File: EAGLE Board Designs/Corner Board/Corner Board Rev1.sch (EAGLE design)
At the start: 7 parts, among them J1 CONNECTOR-4_μF_T_V_BLACK, J2 CONNECTOR-2_MOLEX_NANOFIT_PTH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, J3 CONNECTOR-10_MF_T_V_, J4 CONNECTOR-4_μF_T_V_BLACK, J5 CONNECTOR-4_μF_T_V_BLACK, U1 VOLTAGE_REGULATOR_SOT-89_15V, U2 OPAMP_1_CHANNEL_OPA991

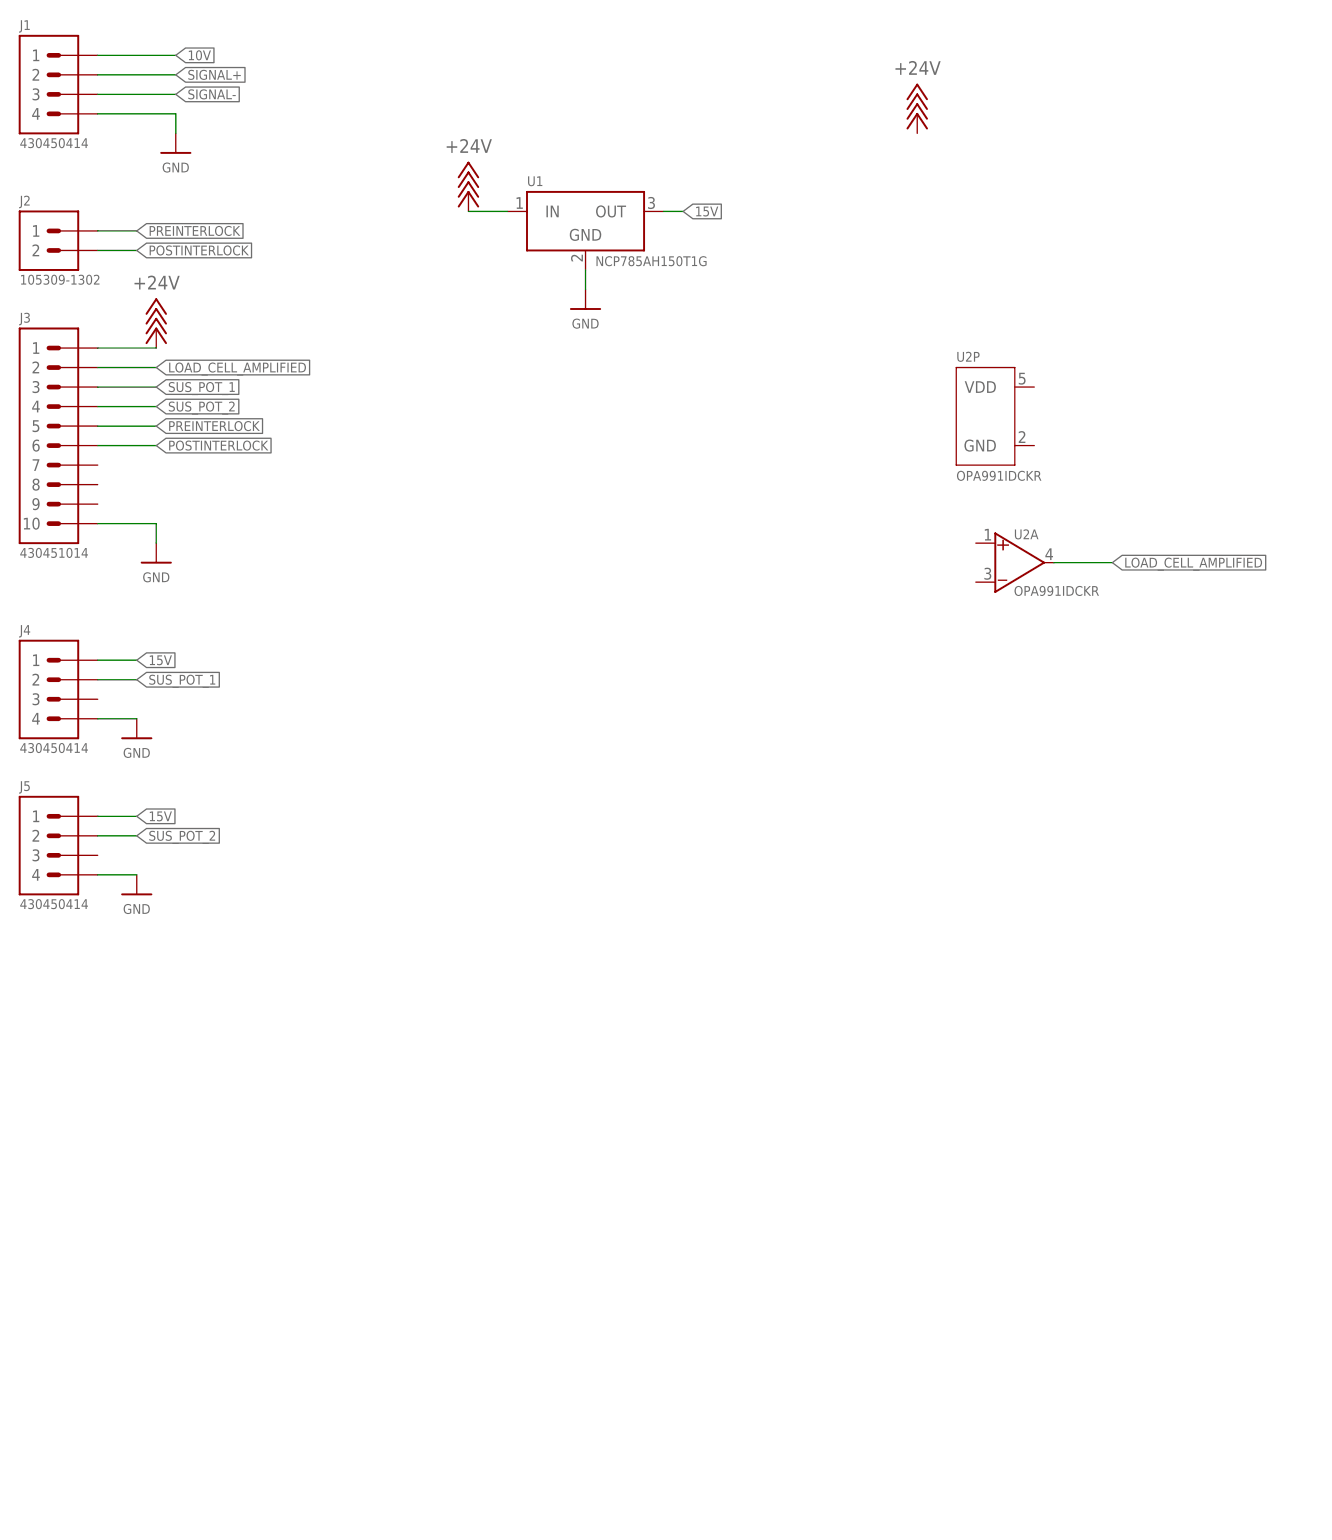
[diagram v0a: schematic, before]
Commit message: added op amps
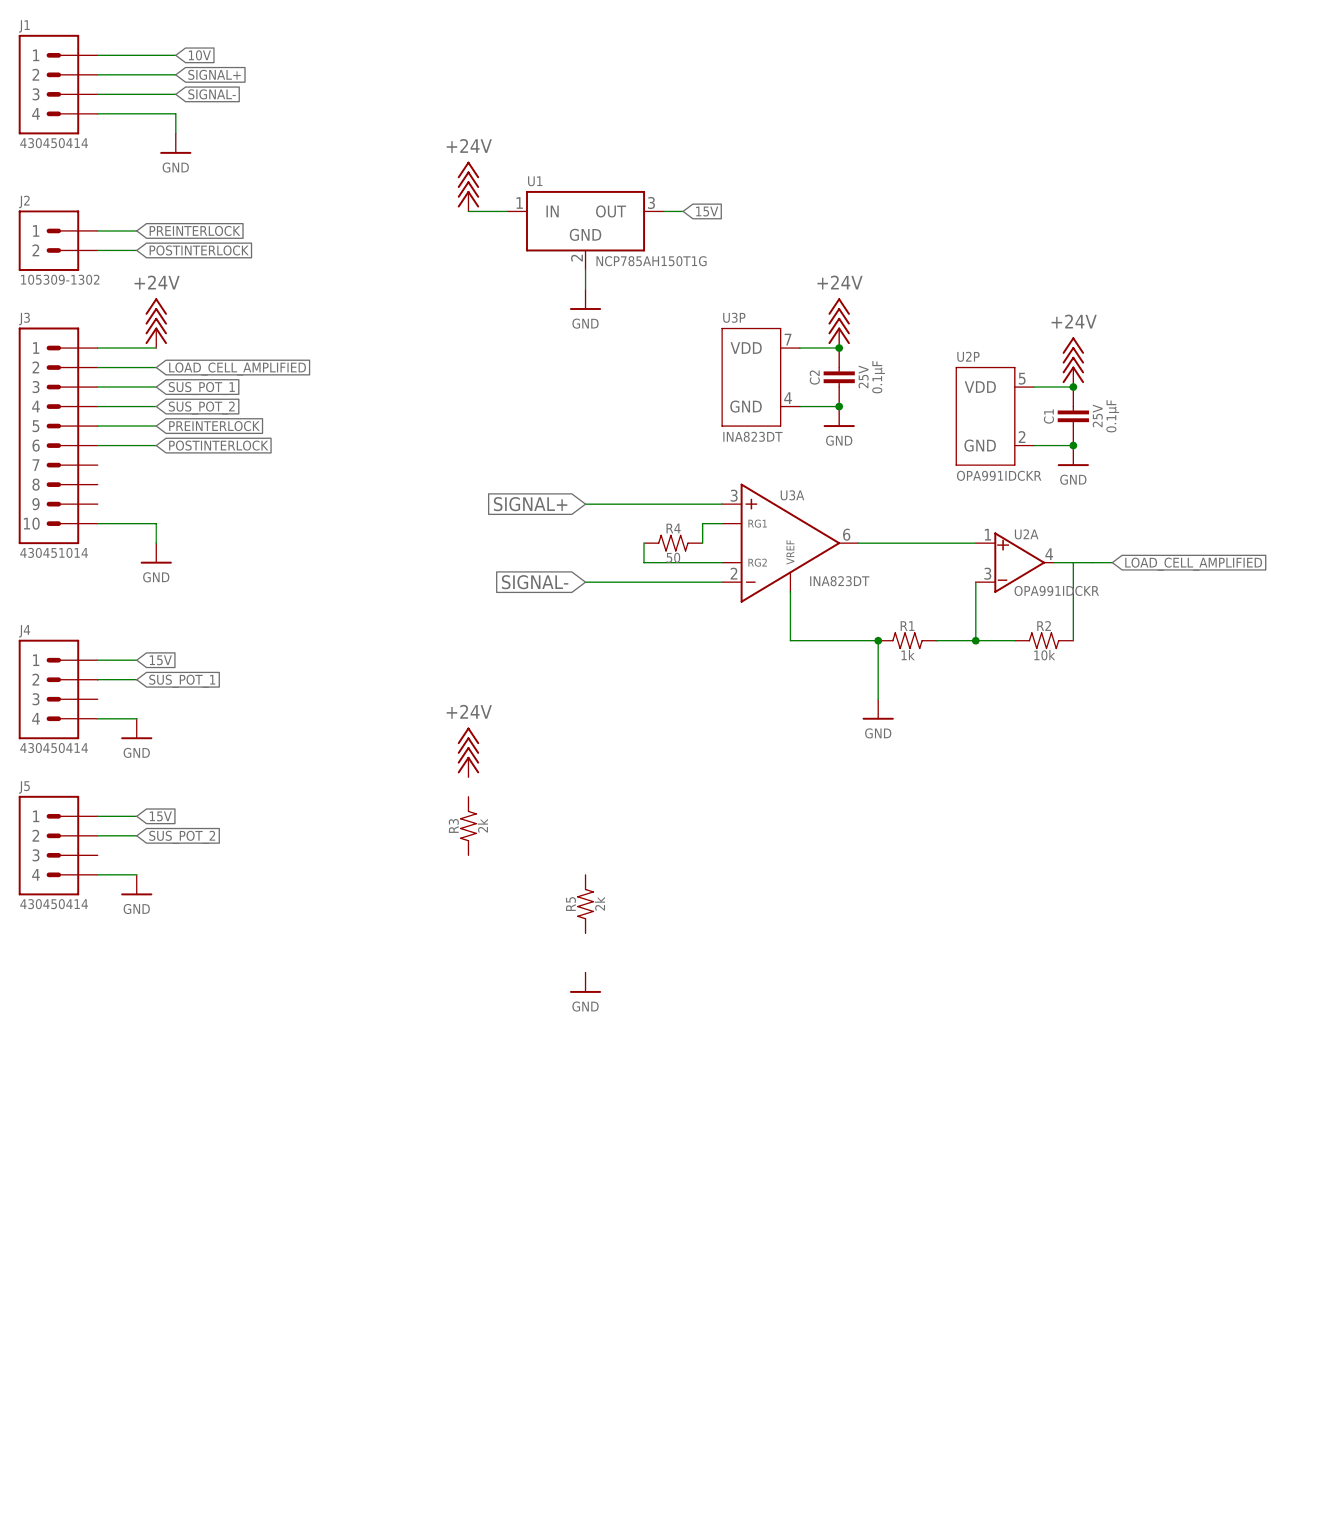
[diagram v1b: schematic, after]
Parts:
- added C1, C2: CAPACITOR_0603_25V_0.1UF, HyTechDevices:CAPACITOR_0603_25V_0.1UF
- added R1: RESISTOR_0603_1K, HyTechDevices:RESISTOR_0603_1K
- added R2: RESISTOR_0603_10K, HyTechDevices:RESISTOR_0603_10K
- added R3, R5: RESISTOR_0603_2K, HyTechDevices:RESISTOR_0603_2K
- added R4: RESISTOR_0603_50, HyTechDevices:RESISTOR_0603_50
- added U3: INA823DT, HyTechDevices:INA823DT
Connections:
- new net N$1: R1.2, R2.1, U2A.VIN-
- new net N$2: R4.2, U3A.RG1
- new net N$3: U2A.VIN+, U3A.VOUT
- new net N$4: R4.1, U3A.RG2
- net +24V: now also C1.1, C2.1, U2P.VDD, U3P.VDD
- net GND: now also C1.2, C2.2, R1.1, U2P.GND, U3A.VREF, U3P.GND
- net LOAD_CELL_AMPLIFIED: now also R2.2
- net SIGNAL+: now also U3A.VIN+
- net SIGNAL-: now also U3A.VIN-
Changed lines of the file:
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@@
 <part name="U2" library="HyTechDevices" deviceset="OPAMP_1_CHANNEL_*" device="" technology="OPA991"/>
 <part name="U$3" library="HyTechSupplies" deviceset="+24V" device=""/>
+<part name="R1" library="HyTechDevices" deviceset="RESISTOR_?_*" device="0603" technology="1K"/>
+<part name="R2" library="HyTechDevices" deviceset="RESISTOR_?_*" device="0603" technology="10K"/>
+<part name="P6" library="HyTechSupplies" deviceset="GND" device=""/>
+<part name="P7" library="HyTechSupplies" deviceset="GND" device=""/>
+<part name="U$4" library="HyTechSupplies" deviceset="+24V" device=""/>
+<part name="C1" library="HyTechDevices" deviceset="CAPACITOR_?_*" device="0603" technology="25V_0.1UF"/>
+<part name="U3" library="HyTechDevices" deviceset="INA823*" device="" technology="DT"/>
+<part name="R3" library="HyTechDevices" deviceset="RESISTOR_?_*" device="0603" technology="2K"/>
+<part name="R4" library="HyTechDevices" deviceset="RESISTOR_?_*" device="0603" technology="50"/>
+<part name="P8" library="HyTechSupplies" deviceset="GND" device=""/>
+<part name="U$5" library="HyTechSupplies" deviceset="+24V" device=""/>
+<part name="C2" library="HyTechDevices" deviceset="CAPACITOR_?_*" device="0603" technology="25V_0.1UF"/>
+<part name="R5" library="HyTechDevices" deviceset="RESISTOR_?_*" device="0603" technology="2K"/>
+<part name="P9" library="HyTechSupplies" deviceset="GND" device=""/>
 </parts>
 <sheets>
@@
 <attribute name="MPN" x="127" y="22.098" size="1.27" layer="95" align="top-left"/>
 </instance>
-<instance part="U$3" gate="G$1" x="121.92" y="68.58" smashed="yes">
-<attribute name="VALUE" x="121.92" y="73.66" size="1.778" layer="96" align="bottom-center"/>
+<instance part="U$3" gate="G$1" x="63.5" y="-15.24" smashed="yes">
+<attribute name="VALUE" x="63.5" y="-10.16" size="1.778" layer="96" align="bottom-center"/>
+</instance>
+<instance part="R1" gate="G$1" x="121.92" y="0" smashed="yes">
+<attribute name="NAME" x="120.65" y="1.27" size="1.27" layer="95" align="bottom-center"/>
+<attribute name="RESISTANCE" x="120.65" y="-1.27" size="1.27" layer="96" align="top-center"/>
+</instance>
+<instance part="R2" gate="G$1" x="139.7" y="0" smashed="yes">
+<attribute name="NAME" x="138.43" y="1.27" size="1.27" layer="95" align="bottom-center"/>
+<attribute name="RESISTANCE" x="138.43" y="-1.27" size="1.27" layer="96" align="top-center"/>
+</instance>
+<instance part="P6" gate="1" x="116.84" y="-10.16" smashed="yes">
+<attribute name="VALUE" x="116.84" y="-11.43" size="1.27" layer="96" align="top-center"/>
+</instance>
+<instance part="P7" gate="1" x="142.24" y="22.86" smashed="yes">
+<attribute name="VALUE" x="142.24" y="21.59" size="1.27" layer="96" align="top-center"/>
+</instance>
+<instance part="U$4" gate="G$1" x="142.24" y="35.56" smashed="yes">
+<attribute name="VALUE" x="142.24" y="40.64" size="1.778" layer="96" align="bottom-center"/>
+</instance>
+<instance part="C1" gate="G$1" x="142.24" y="30.48" smashed="yes" rot="R90">
+<attribute name="NAME" x="139.7" y="29.21" size="1.27" layer="95" rot="R90" align="bottom-center"/>
+<attribute name="VOLTAGE" x="144.78" y="29.21" size="1.27" layer="96" rot="R90" align="top-center"/>
+<attribute name="CAPACITANCE" x="146.558" y="29.21" size="1.27" layer="96" rot="R90" align="top-center"/>
+</instance>
+<instance part="U3" gate="A" x="99.06" y="12.7" smashed="yes">
+<attribute name="NAME" x="104.013" y="18.288" size="1.27" layer="95"/>
+<attribute name="MPN" x="107.823" y="8.382" size="1.27" layer="96" align="top-left"/>
+</instance>
+<instance part="U3" gate="P" x="96.52" y="40.64" smashed="yes">
+<attribute name="NAME" x="96.52" y="41.402" size="1.27" layer="95"/>
+<attribute name="MPN" x="96.52" y="27.178" size="1.27" layer="95" align="top-left"/>
+</instance>
+<instance part="R3" gate="G$1" x="63.5" y="-22.86" smashed="yes" rot="R90">
+<attribute name="NAME" x="62.23" y="-24.13" size="1.27" layer="95" rot="R90" align="bottom-center"/>
+<attribute name="RESISTANCE" x="64.77" y="-24.13" size="1.27" layer="96" rot="R90" align="top-center"/>
+</instance>
+<instance part="R4" gate="G$1" x="91.44" y="12.7" smashed="yes">
+<attribute name="NAME" x="90.17" y="13.97" size="1.27" layer="95" align="bottom-center"/>
+<attribute name="RESISTANCE" x="90.17" y="11.43" size="1.27" layer="96" align="top-center"/>
+</instance>
+<instance part="P8" gate="1" x="111.76" y="27.94" smashed="yes">
+<attribute name="VALUE" x="111.76" y="26.67" size="1.27" layer="96" align="top-center"/>
+</instance>
+<instance part="U$5" gate="G$1" x="111.76" y="40.64" smashed="yes">
+<attribute name="VALUE" x="111.76" y="45.72" size="1.778" layer="96" align="bottom-center"/>
+</instance>
+<instance part="C2" gate="G$1" x="111.76" y="35.56" smashed="yes" rot="R90">
+<attribute name="NAME" x="109.22" y="34.29" size="1.27" layer="95" rot="R90" align="bottom-center"/>
+<attribute name="VOLTAGE" x="114.3" y="34.29" size="1.27" layer="96" rot="R90" align="top-center"/>
+<attribute name="CAPACITANCE" x="116.078" y="34.29" size="1.27" layer="96" rot="R90" align="top-center"/>
+</instance>
+<instance part="R5" gate="G$1" x="78.74" y="-33.02" smashed="yes" rot="R90">
+<attribute name="NAME" x="77.47" y="-34.29" size="1.27" layer="95" rot="R90" align="bottom-center"/>
+<attribute name="RESISTANCE" x="80.01" y="-34.29" size="1.27" layer="96" rot="R90" align="top-center"/>
+</instance>
+<instance part="P9" gate="1" x="78.74" y="-45.72" smashed="yes">
+<attribute name="VALUE" x="78.74" y="-46.99" size="1.27" layer="96" align="top-center"/>
 </instance>
 </instances>
@@
 <pinref part="P5" gate="1" pin="GND"/>
 </segment>
+<segment>
+<pinref part="R1" gate="G$1" pin="1"/>
+<wire x1="116.84" y1="0" x2="116.84" y2="-7.62" width="0.1524" layer="91"/>
+<pinref part="P6" gate="1" pin="GND"/>
+<pinref part="U3" gate="A" pin="VREF"/>
+<wire x1="105.41" y1="6.35" x2="105.41" y2="0" width="0.1524" layer="91"/>
+<wire x1="105.41" y1="0" x2="116.84" y2="0" width="0.1524" layer="91"/>
+<junction x="116.84" y="0"/>
+</segment>
+<segment>
+<pinref part="P7" gate="1" pin="GND"/>
+<pinref part="C1" gate="G$1" pin="2"/>
+<pinref part="U2" gate="P" pin="GND"/>
+<wire x1="137.16" y1="25.4" x2="142.24" y2="25.4" width="0.1524" layer="91"/>
+<junction x="142.24" y="25.4"/>
+</segment>
+<segment>
+<pinref part="P8" gate="1" pin="GND"/>
+<pinref part="C2" gate="G$1" pin="2"/>
+<wire x1="106.68" y1="30.48" x2="111.76" y2="30.48" width="0.1524" layer="91"/>
+<junction x="111.76" y="30.48"/>
+<pinref part="U3" gate="P" pin="GND"/>
+</segment>
 </net>
 <net name="SIGNAL+" class="0">
@@
 <label x="25.4" y="73.66" size="1.27" layer="95" xref="yes"/>
 </segment>
+<segment>
+<pinref part="U3" gate="A" pin="VIN+"/>
+<wire x1="96.52" y1="17.78" x2="78.74" y2="17.78" width="0.1524" layer="91"/>
+<label x="78.74" y="17.78" size="1.778" layer="95" rot="R180" xref="yes"/>
+</segment>
 </net>
 <net name="SIGNAL-" class="0">
@@
 <label x="25.4" y="71.12" size="1.27" layer="95" xref="yes"/>
 </segment>
+<segment>
+<pinref part="U3" gate="A" pin="VIN-"/>
+<wire x1="96.52" y1="7.62" x2="78.74" y2="7.62" width="0.1524" layer="91"/>
+<label x="78.74" y="7.62" size="1.778" layer="95" rot="R180" xref="yes"/>
+</segment>
 </net>
 <net name="PREINTERLOCK" class="0">
@@
 <pinref part="U$2" gate="G$1" pin="+24V"/>
 </segment>
+<segment>
+<pinref part="U$4" gate="G$1" pin="+24V"/>
+<pinref part="C1" gate="G$1" pin="1"/>
+<pinref part="U2" gate="P" pin="VDD"/>
+<wire x1="137.16" y1="33.02" x2="142.24" y2="33.02" width="0.1524" layer="91"/>
+<junction x="142.24" y="33.02"/>
+</segment>
+<segment>
+<pinref part="U$5" gate="G$1" pin="+24V"/>
+<pinref part="C2" gate="G$1" pin="1"/>
+<wire x1="106.68" y1="38.1" x2="111.76" y2="38.1" width="0.1524" layer="91"/>
+<junction x="111.76" y="38.1"/>
+<pinref part="U3" gate="P" pin="VDD"/>
+</segment>
 </net>
 <net name="LOAD_CELL_AMPLIFIED" class="0">
@@
 <segment>
 <pinref part="U2" gate="A" pin="VOUT"/>
-<wire x1="139.7" y1="10.16" x2="147.32" y2="10.16" width="0.1524" layer="91"/>
+<wire x1="139.7" y1="10.16" x2="142.24" y2="10.16" width="0.1524" layer="91"/>
 <label x="147.32" y="10.16" size="1.27" layer="95" xref="yes"/>
+<pinref part="R2" gate="G$1" pin="2"/>
+<wire x1="144.78" y1="10.16" x2="147.32" y2="10.16" width="0.1524" layer="91"/>
+<wire x1="144.78" y1="10.16" x2="142.24" y2="10.16" width="0.1524" layer="91"/>
+<wire x1="142.24" y1="10.16" x2="142.24" y2="0" width="0.1524" layer="91"/>
 </segment>
 </net>
@@
 </segment>
 </net>
+<net name="N$1" class="0">
+<segment>
+<pinref part="U2" gate="A" pin="VIN-"/>
+<wire x1="129.54" y1="7.62" x2="129.54" y2="0" width="0.1524" layer="91"/>
+<pinref part="R2" gate="G$1" pin="1"/>
+<wire x1="129.54" y1="0" x2="134.62" y2="0" width="0.1524" layer="91"/>
+<pinref part="R1" gate="G$1" pin="2"/>
+<wire x1="129.54" y1="0" x2="124.46" y2="0" width="0.1524" layer="91"/>
+<junction x="129.54" y="0"/>
+</segment>
+</net>
+<net name="N$3" class="0">
+<segment>
+<pinref part="U2" gate="A" pin="VIN+"/>
+<wire x1="129.54" y1="12.7" x2="114.3" y2="12.7" width="0.1524" layer="91"/>
+<pinref part="U3" gate="A" pin="VOUT"/>
+</segment>
+</net>
+<net name="N$2" class="0">
+<segment>
+<pinref part="R4" gate="G$1" pin="2"/>
+<pinref part="U3" gate="A" pin="RG1"/>
+<wire x1="93.98" y1="12.7" x2="93.98" y2="15.24" width="0.1524" layer="91"/>
+<wire x1="93.98" y1="15.24" x2="96.52" y2="15.24" width="0.1524" layer="91"/>
+</segment>
+</net>
+<net name="N$4" class="0">
+<segment>
+<pinref part="R4" gate="G$1" pin="1"/>
+<pinref part="U3" gate="A" pin="RG2"/>
+<wire x1="86.36" y1="12.7" x2="86.36" y2="10.16" width="0.1524" layer="91"/>
+<wire x1="86.36" y1="10.16" x2="96.52" y2="10.16" width="0.1524" layer="91"/>
+</segment>
+</net>
